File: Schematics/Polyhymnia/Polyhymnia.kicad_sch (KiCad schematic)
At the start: 52 parts, among them J1 AudioShield, SW1 Filter Cutoff, SW2 Filter Resonance, SW3 OSC1 Type, SW4 OSC1 Detune, SW5 Filter Resonance, SW6 OSC2 Type, SW7 OSC2 Detune, SW8 OSC3 Type, SW9 OSC3 Detune, U1 Teensy4.1, U2 74HC595, U3 74HC595, U4 74HC595, U5 74HC595, U6 ATmega32-16P

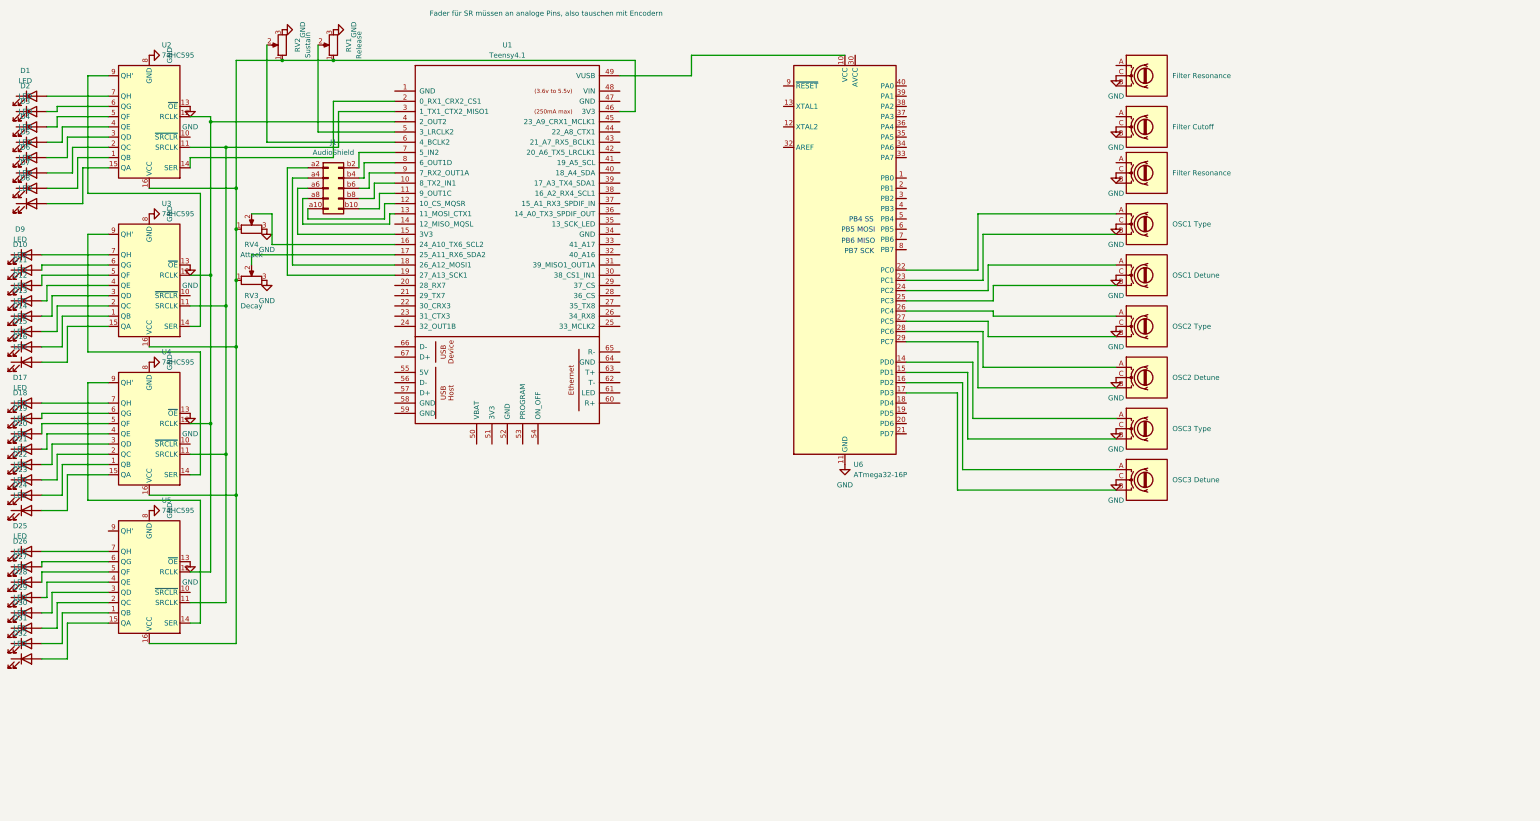
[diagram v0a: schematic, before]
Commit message: Pulled parts into hierarchical schematics
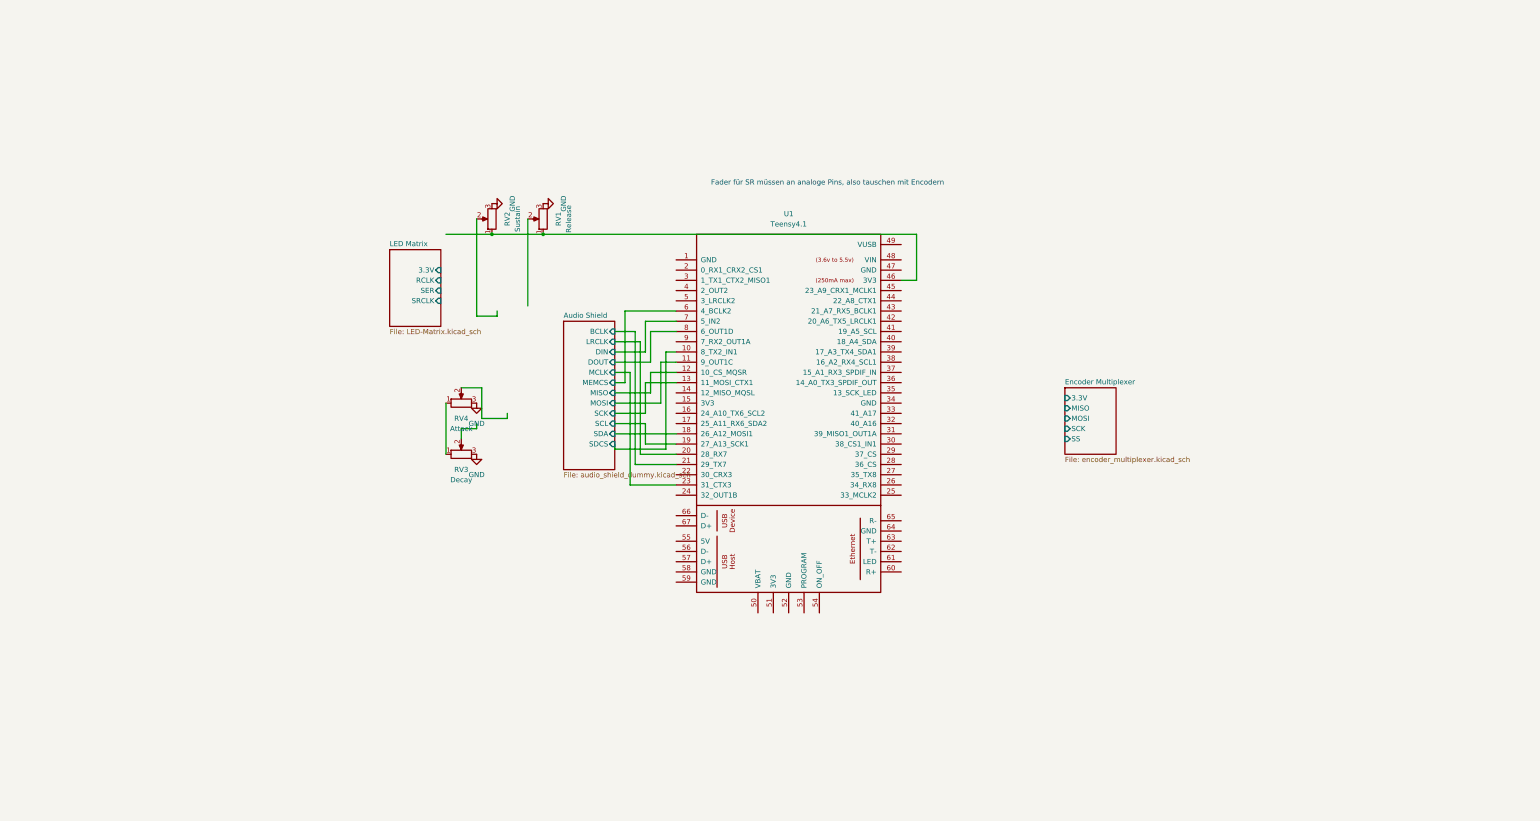
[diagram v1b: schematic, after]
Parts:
- removed D1, D10, D11, D12, D13, D14, D15, D16, D17, D18, D19, D2, D20, D21, D22, D23, D24, D25, D26, D27, D28, D29, D3, D30, D31, D32, D4, D5, D6, D7, D8, D9: LED, symbol Device:LED
- removed J1: AudioShield, symbol Connector:DIN41612_02x05_AB_EvenPins
- removed SW1: Filter Cutoff, symbol Device:RotaryEncoder
- removed SW2, SW5: Filter Resonance, symbol Device:RotaryEncoder
- removed SW3: OSC1 Type, symbol Device:RotaryEncoder
- removed SW4: OSC1 Detune, symbol Device:RotaryEncoder
- removed SW6: OSC2 Type, symbol Device:RotaryEncoder
- removed SW7: OSC2 Detune, symbol Device:RotaryEncoder
- removed SW8: OSC3 Type, symbol Device:RotaryEncoder
- removed SW9: OSC3 Detune, symbol Device:RotaryEncoder
- removed U2, U3, U4, U5: 74HC595, symbol 74xx:74HC595
- removed U6: ATmega32-16P, Package_DIP:DIP-40_W15.24mm, symbol MCU_Microchip_ATmega:ATmega32-16P
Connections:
- net at RV1.1, RV2.1, U1.46 (3V3): no longer RV3.1, RV4.1
- net Audio Shield/MISO: now reaches U1.12 (10_CS_MQSR)
- net Audio Shield/SCL: now reaches U1.19 (27_A13_SCK1)
- net Audio Shield/SDA: now reaches U1.18 (26_A12_MOSI1)
- net Audio Shield/SCK: now reaches U1.13 (11_MOSI_CTX1)
- net Audio Shield/MOSI: now reaches U1.11 (9_OUT1C)
- net Audio Shield/DIN: now reaches U1.7 (5_IN2)
- net Audio Shield/DOUT: now reaches U1.8 (6_OUT1D)
- net Audio Shield/SDCS: now reaches U1.10 (8_TX2_IN1)
- net at RV1.2: no longer U1.5 (3_LRCLK2)
- net at U1.16 (24_A10_TX6_SCL2): no longer RV4.2
- net at U1.17 (25_A11_RX6_SDA2): no longer RV3.2
- net Audio Shield/LRCLK: now reaches U1.20 (28_RX7)
- net Audio Shield/BCLK: now reaches U1.21 (29_TX7)
- net Audio Shield/MCLK: now reaches U1.23 (31_CTX3)
- net at RV2.2: no longer U1.6 (4_BCLK2)
- new net: RV3.1, RV4.1
- new net Audio Shield/MEMCS: U1.6 (4_BCLK2)
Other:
- added sheet Audio Shield (audio_shield_dummy.kicad_sch)
- added sheet Encoder Multiplexer (encoder_multiplexer.kicad_sch)
- added sheet LED Matrix (LED-Matrix.kicad_sch)
- note removed: "PB4 SS"
- note removed: "PB5 MOSI"
- note removed: "PB6 MISO"
- note removed: "PB7 SCK"
- title: (none) -> Polyhymnia
- moved on the sheet: RV1, RV2, RV3, RV4, U1

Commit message: Cleaned up wiring
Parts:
- removed RV1: Release, symbol Device:R_Potentiometer
- removed RV2: Sustain, symbol Device:R_Potentiometer
- removed RV3: Decay, symbol Device:R_Potentiometer
- removed RV4: Attack, symbol Device:R_Potentiometer
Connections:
- net Encoder Multiplexer/SS: now also U1.2 (0_RX1_CRX2_CS1)
- net +5V: now reaches U1.49 (VUSB)
- net Audio Shield/BCLK renamed AudioShield_BCLK
- net Audio Shield/DIN renamed AudioShield_DIN
- net Audio Shield/DOUT renamed AudioShield_DOUT
- net Audio Shield/LRCLK renamed AudioShield_LRCLK
- net Audio Shield/MCLK renamed AudioShield_MCLK
- net Audio Shield/MEMCS renamed AudioShield_MEMCS
- net Audio Shield/MISO renamed AudioShield_MISO
- net Audio Shield/MOSI renamed AudioShield_MOSI
- net Audio Shield/SCK renamed AudioShield_SCK
- net Audio Shield/SCL renamed AudioShield_SCL
- net Audio Shield/SDA renamed AudioShield_SDA
- net Audio Shield/SDCS renamed AudioShield_SDCS
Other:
- removed sheet Audio Shield

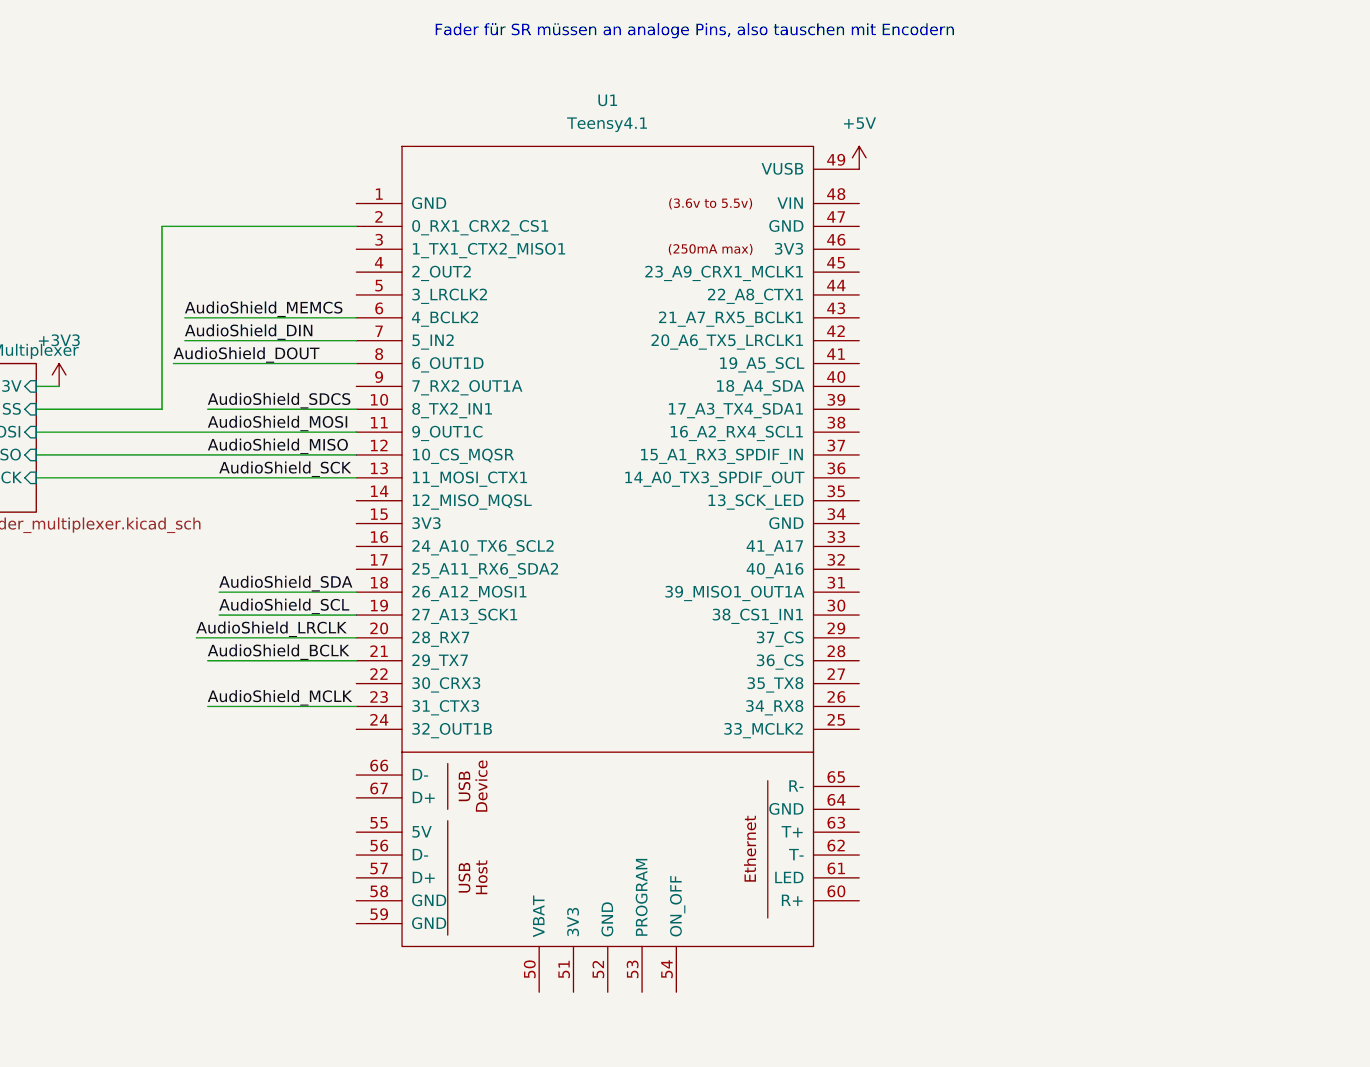
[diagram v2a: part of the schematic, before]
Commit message: Added MIDI in to schematics
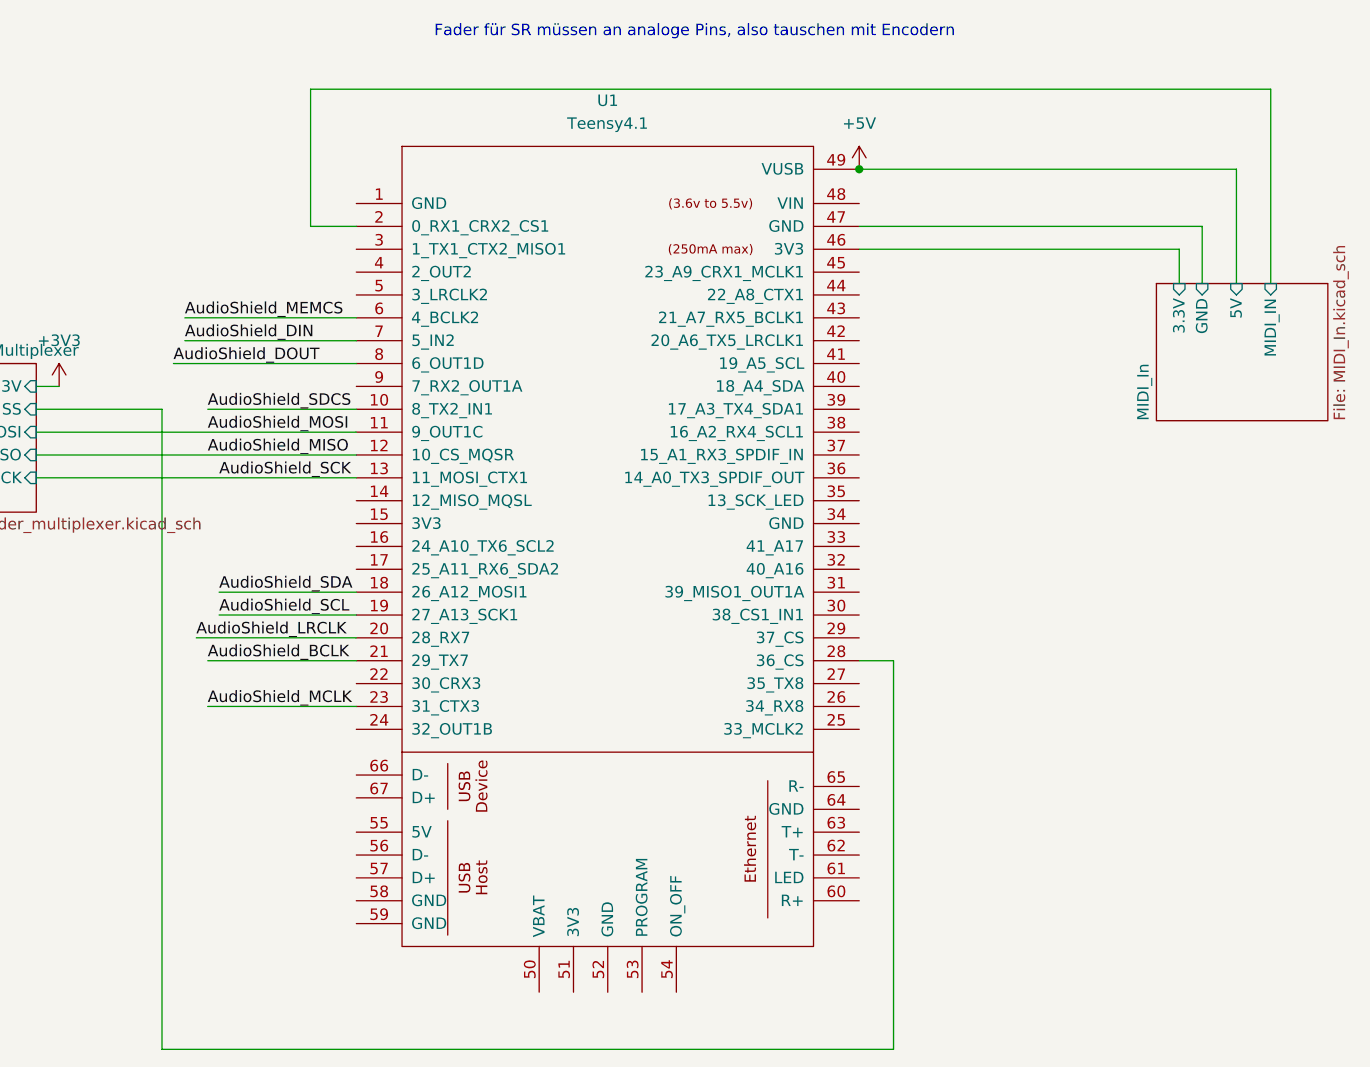
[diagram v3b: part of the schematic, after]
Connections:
- net Encoder Multiplexer/SS: now also U1.28 (36_CS); no longer U1.2 (0_RX1_CRX2_CS1)
- net MIDI_In/3.3V: now reaches U1.46 (3V3)
- net MIDI_In/GND: now reaches U1.47 (GND)
- new net MIDI_In/MIDI_IN: U1.2 (0_RX1_CRX2_CS1)
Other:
- added sheet MIDI_In (MIDI_In.kicad_sch)
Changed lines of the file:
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@@
+		)
+	)
+	(junction
+		(at 232.41 82.55)
+		(diameter 0)
+		(color 0 0 0 0)
+	)
+	(wire
+		(pts
+			(xy 236.22 180.34) (xy 236.22 137.16)
+		)
+		(stroke
+			(width 0)
+			(type default)
+		)
+	)
+	(wire
+		(pts
+			(xy 232.41 91.44) (xy 267.97 91.44)
+		)
+		(stroke
+			(width 0)
+			(type default)
+		)
+	)
+	(wire
+		(pts
+			(xy 267.97 95.25) (xy 267.97 91.44)
+		)
+		(stroke
+			(width 0)
+			(type default)
 		)
 	)
@@
 	(wire
 		(pts
+			(xy 274.32 95.25) (xy 274.32 82.55)
+		)
+		(stroke
+			(width 0)
+			(type default)
+		)
+	)
+	(wire
+		(pts
 			(xy 157.48 101.6) (xy 176.53 101.6)
 		)
@@
 	(wire
 		(pts
+			(xy 154.94 180.34) (xy 236.22 180.34)
+		)
+		(stroke
+			(width 0)
+			(type default)
+		)
+	)
+	(wire
+		(pts
+			(xy 171.45 88.9) (xy 176.53 88.9)
+		)
+		(stroke
+			(width 0)
+			(type default)
+		)
+	)
+	(wire
+		(pts
 			(xy 140.97 109.22) (xy 154.94 109.22)
 		)
@@
 	(wire
 		(pts
-			(xy 154.94 109.22) (xy 154.94 88.9)
-		)
-		(stroke
-			(width 0)
-			(type default)
-		)
-	)
-	(wire
-		(pts
-			(xy 154.94 88.9) (xy 176.53 88.9)
+			(xy 154.94 109.22) (xy 154.94 180.34)
 		)
 		(stroke
@@
 	(wire
 		(pts
+			(xy 270.51 95.25) (xy 270.51 88.9)
+		)
+		(stroke
+			(width 0)
+			(type default)
+		)
+	)
+	(wire
+		(pts
+			(xy 171.45 73.66) (xy 278.13 73.66)
+		)
+		(stroke
+			(width 0)
+			(type default)
+		)
+	)
+	(wire
+		(pts
 			(xy 158.75 134.62) (xy 176.53 134.62)
 		)
@@
 	(wire
 		(pts
+			(xy 278.13 95.25) (xy 278.13 73.66)
+		)
+		(stroke
+			(width 0)
+			(type default)
+		)
+	)
+	(wire
+		(pts
 			(xy 157.48 99.06) (xy 176.53 99.06)
 		)
@@
 	(wire
 		(pts
+			(xy 236.22 137.16) (xy 232.41 137.16)
+		)
+		(stroke
+			(width 0)
+			(type default)
+		)
+	)
+	(wire
+		(pts
+			(xy 274.32 82.55) (xy 232.41 82.55)
+		)
+		(stroke
+			(width 0)
+			(type default)
+		)
+	)
+	(wire
+		(pts
 			(xy 160.02 137.16) (xy 176.53 137.16)
 		)
@@
 		(pts
 			(xy 160.02 142.24) (xy 176.53 142.24)
+		)
+		(stroke
+			(width 0)
+			(type default)
+		)
+	)
+	(wire
+		(pts
+			(xy 171.45 73.66) (xy 171.45 88.9)
+		)
+		(stroke
+			(width 0)
+			(type default)
+		)
+	)
+	(wire
+		(pts
+			(xy 270.51 88.9) (xy 232.41 88.9)
 		)
 		(stroke
@@
 				)
 			)
+		)
+	)
+	(sheet
+		(at 265.43 95.25)
+		(size 19.05 15.24)
+		(exclude_from_sim no)
+		(in_bom yes)
+		(on_board yes)
+		(dnp no)
+		(fields_autoplaced yes)
+		(stroke
+			(width 0.1524)
+			(type solid)
+		)
+		(fill
+			(color 0 0 0 0)
+		)
+		(property "Sheetname" "MIDI_In"
+			(at 264.7184 110.49 90)
+			(show_name no)
+			(do_not_autoplace no)
+			(effects
+				(font
+					(size 1.27 1.27)
+				)
+				(justify left bottom)
+			)
+		)
+		(property "Sheetfile" "MIDI_In.kicad_sch"
+			(at 285.0646 110.49 90)
+			(show_name no)
+			(do_not_autoplace no)
+			(effects
+				(font
+					(size 1.27 1.27)
+				)
+				(justify left top)
+			)
+		)
+		(pin "MIDI_IN" input
+			(at 278.13 95.25 90)
+			(effects
+				(font
+					(size 1.27 1.27)
+				)
+				(justify right)
+			)
+		)
+		(pin "3.3V" input
+			(at 267.97 95.25 90)
+			(effects
+				(font
+					(size 1.27 1.27)
+				)
+				(justify right)
+			)
+		)
+		(pin "5V" input
+			(at 274.32 95.25 90)
+			(effects
+				(font
+					(size 1.27 1.27)
+				)
+				(justify right)
+			)
+		)
+		(pin "GND" input
+			(at 270.51 95.25 90)
+			(effects
+				(font
+					(size 1.27 1.27)
+				)
+				(justify right)
+			)
+		)
+		(instances
+			(project "Polyhymnia"
+				(path "/e4936a91-9e28-4906-9468-02ad94b9239b"
+					(page "4")
+				)
+			)

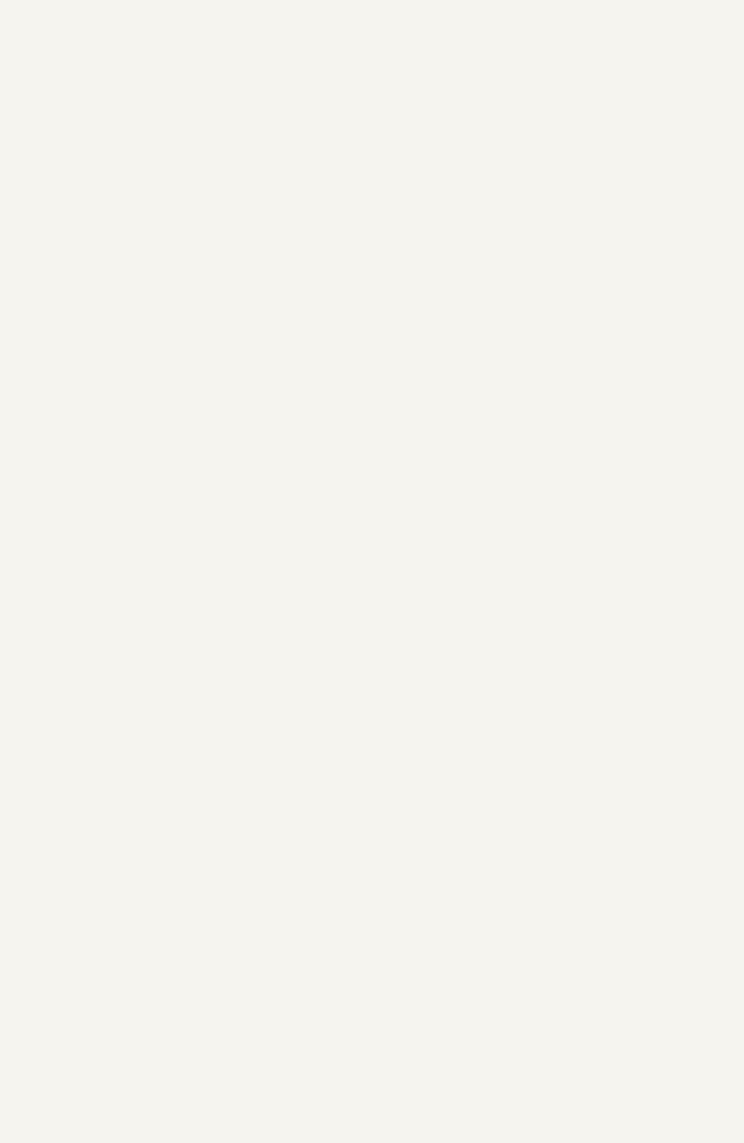
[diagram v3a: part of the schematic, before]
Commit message: Added schematics for filter, fader and envelope modules
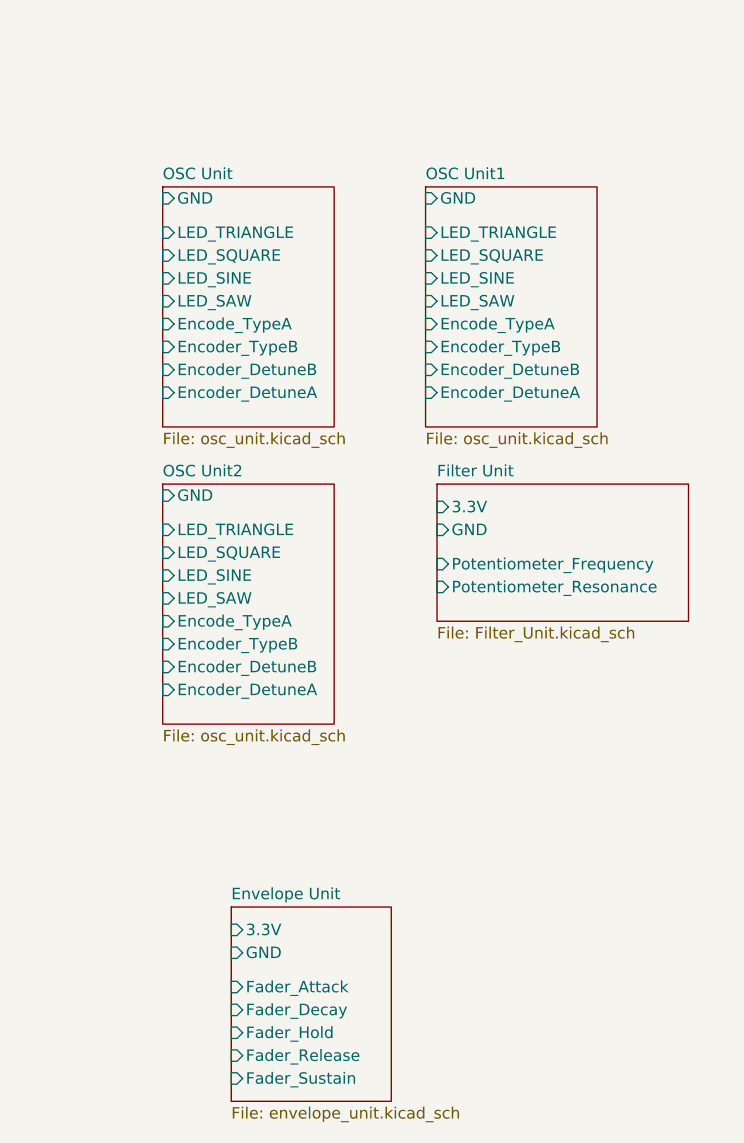
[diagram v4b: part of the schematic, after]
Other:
- added sheet Envelope Unit (envelope_unit.kicad_sch)
- added sheet Filter Unit (Filter_Unit.kicad_sch)
- added sheet OSC Unit (osc_unit.kicad_sch)
- added sheet OSC Unit1 (osc_unit.kicad_sch)
- added sheet OSC Unit2 (osc_unit.kicad_sch)
